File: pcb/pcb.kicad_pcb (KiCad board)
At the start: 2 copper layers, 145.2 x 98.5 mm, 105 parts, among them J1 OLED Connector, J2 Tag connect TC2030-CTX, J3 USB C 2.0 Connector, J4 Conn_01x01_Socket, J5 Conn_01x01_Socket, Q1 BSS84, Q2 BSS138, SW1 RESET, SW10 SW_Push, SW11 SW_Push, SW12 SW_Push, SW13 SW_Push, SW14 SW_Push, SW15 SW_Push, SW16 SW_Push, SW17 SW_Push, SW18 SW_Push, SW19 SW_Push, SW2 SW_Push, SW20 SW_Push, SW21 SW_Push, SW22 SW_Push, SW23 EC11 Encoder, SW24 ON/OFF, SW3 SW_Push, SW4 SW_Push, SW5 SW_Push, SW6 SW_Push, SW7 SW_Push, SW8 SW_Push, SW9 SW_Push, U1 nRF52840, U2 BQ24073RGT, U3 USBLC6-2SC6, U4 DRV2605LDGS, Y1 32MHz, Y2 32.768kHz

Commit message: finished routing second half
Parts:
- added AE2: Antenna_Shield, kbd:BLE_ANTENNA, B.Cu at (222.5, 141.9)
- added BT3: Lipo Cell, Connector_JST:JST_PH_S2B-PH-SM4-TB_1x02-1MP_P2.00mm_Horizontal, F.Cu at (241.9, 102.6)
- added C32: 1.2p, Capacitor_SMD:C_0402_1005Metric, F.Cu at (228.6, 141.5)
- added C33: 8p, Capacitor_SMD:C_0402_1005Metric, F.Cu at (232.3, 143.8)
- added C34: 8p, Capacitor_SMD:C_0402_1005Metric, F.Cu at (238.1, 142.1)
- added C35: 1p, Capacitor_SMD:C_0402_1005Metric, F.Cu at (230.7, 139.4)
- added C36: 8p, Capacitor_SMD:C_0402_1005Metric, F.Cu at (241.4, 132.8)
- added C37: 8p, Capacitor_SMD:C_0402_1005Metric, F.Cu at (240.1, 131.4)
- added C38: 100n, Capacitor_SMD:C_0402_1005Metric, F.Cu at (242.4, 134.6)
- added C40: 100p, Capacitor_SMD:C_0402_1005Metric, F.Cu at (231.9, 141.3)
- added C42: 47n, Capacitor_SMD:C_0402_1005Metric, F.Cu at (238.8, 137.0)
- added C43: 1u, Capacitor_SMD:C_0603_1608Metric, F.Cu at (240.1, 136.5)
- added C45: 4u7, Capacitor_SMD:C_0805_2012Metric, F.Cu at (233.1, 126.8)
- added C46: 1u, Capacitor_SMD:C_0603_1608Metric, F.Cu at (223.1, 118.0)
- added C47: 4u7, Capacitor_SMD:C_0805_2012Metric, F.Cu at (235.6, 128.4)
- added C48: 1u, Capacitor_SMD:C_0603_1608Metric, F.Cu at (236.6, 140.1)
- added C49: 100n, Capacitor_SMD:C_0402_1005Metric, F.Cu at (236.2, 130.0)
- added C50: 100n, Capacitor_SMD:C_0402_1005Metric, F.Cu at (229.2, 131.3)
- added C51: 100n, Capacitor_SMD:C_0402_1005Metric, F.Cu at (227.4, 133.8)
- added C52: 4u7, Capacitor_SMD:C_0805_2012Metric, F.Cu at (231.3, 128.0)
- added C53: 1u, Capacitor_SMD:C_0603_1608Metric, F.Cu at (232.6, 103.9)
- added C54: 4u7, Capacitor_SMD:C_0805_2012Metric, F.Cu at (228.3, 111.3)
- added C55: 4u7, Capacitor_SMD:C_0805_2012Metric, F.Cu at (235.4, 102.5)
- added C56: 100n, Capacitor_SMD:C_0402_1005Metric, F.Cu at (245.1, 108.6)
- added D43: 1N4148W, Diode_SMD:D_SOD-123, F.Cu at (252.9, 117.1)
- added D44: 1N4148W, Diode_SMD:D_SOD-123, F.Cu at (267.3, 115.5)
- added D45: 1N4148W, Diode_SMD:D_SOD-123, F.Cu at (286.1, 112.6)
- added D46: 1N4148W, Diode_SMD:D_SOD-123, F.Cu at (305.1, 112.7)
- added D47: 1N4148W, Diode_SMD:D_SOD-123, F.Cu at (324.1, 115.3)
- added D48: 1N4148W, Diode_SMD:D_SOD-123, F.Cu at (342.9, 115.9)
- added D49: 1N4148W, Diode_SMD:D_SOD-123, F.Cu at (253.3, 136.1)
- added D50: 1N4148W, Diode_SMD:D_SOD-123, F.Cu at (266.7, 134.7)
- added D51: 1N4148W, Diode_SMD:D_SOD-123, F.Cu at (285.5, 131.5)
- added D52: 1N4148W, Diode_SMD:D_SOD-123, F.Cu at (304.7, 132.1)
- added D53: 1N4148W, Diode_SMD:D_SOD-123, F.Cu at (323.9, 134.7)
- added D54: 1N4148W, Diode_SMD:D_SOD-123, F.Cu at (342.7, 134.7)
- added D55: 1N4148W, Diode_SMD:D_SOD-123, F.Cu at (248.4, 153.4)
- added D56: 1N4148W, Diode_SMD:D_SOD-123, F.Cu at (267.3, 153.5)
- added D57: 1N4148W, Diode_SMD:D_SOD-123, F.Cu at (286.1, 150.9)
- added D58: 1N4148W, Diode_SMD:D_SOD-123, F.Cu at (305.3, 151.3)
- added D59: 1N4148W, Diode_SMD:D_SOD-123, F.Cu at (324.1, 153.7)
- added D60: 1N4148W, Diode_SMD:D_SOD-123, F.Cu at (342.9, 153.9)
- added D61: 1N4148W, Diode_SMD:D_SOD-123, F.Cu at (227.9, 186.9)
- added D62: 1N4148W, Diode_SMD:D_SOD-123, F.Cu at (246.5, 178.9)
- added D63: 1N4148W, Diode_SMD:D_SOD-123, F.Cu at (266.9, 174.7)
- added H10: MountingHole, MountingHole:MountingHole_2.2mm_M2, F.Cu at (340.3, 141.7)
- added H6: MountingHole, MountingHole:MountingHole_2.2mm_M2, F.Cu at (238.8, 167.6)
- added H7: MountingHole, MountingHole:MountingHole_2.2mm_M2, F.Cu at (264.3, 105.7)
- added H8: MountingHole, MountingHole:MountingHole_2.2mm_M2, F.Cu at (264.3, 141.7)
- added H9: MountingHole, MountingHole:MountingHole_2.2mm_M2, F.Cu at (340.3, 105.7)
- added J10: Tag connect TC2030-CTX, Connector_PinHeader_2.54mm:PinHeader_2x03_P2.54mm_Vertical, F.Cu at (220.4, 130.0)
- added J11: USB C 2.0 Connector, kbd:TYPE-C-31-M-13C, F.Cu at (224.9, 99.1)
- added J7: OLED Connector, kbd:OLED, F.Cu at (231.8, 145.6)
- added J8: Conn_01x01_Socket, kbd:TE_2199248-6, F.Cu at (230.5, 118.9)
- added J9: Conn_01x01_Socket, kbd:TE_2199248-6, F.Cu at (231.4, 122.6)
- added L10: 2.2nH, Inductor_SMD:L_0402_1005Metric, F.Cu at (227.2, 142.1)
- added L4: 4.7nH, Inductor_SMD:L_0402_1005Metric, F.Cu at (229.3, 140.1)
- added L6: 10uH, Inductor_SMD:L_0603_1608Metric, F.Cu at (241.7, 135.8)
- added L7: 10uH, Inductor_SMD:L_0603_1608Metric, F.Cu at (234.5, 125.5)
- added L8: 15nH, Inductor_SMD:L_0402_1005Metric, F.Cu at (243.0, 137.4)
- added Q5: BSS84, Package_TO_SOT_SMD:SOT-23, F.Cu at (241.3, 109.1)
- added Q6: BSS138, Package_TO_SOT_SMD:SOT-23, F.Cu at (233.9, 113.9)
- added R21: 2k2, Resistor_SMD:R_0402_1005Metric, F.Cu at (223.3, 126.1)
- added R22: 2k2, Resistor_SMD:R_0402_1005Metric, F.Cu at (220.7, 119.6)
- added R23: 100k, Resistor_SMD:R_0603_1608Metric, F.Cu at (241.0, 111.7)
- added R24: 5k1, Resistor_SMD:R_0402_1005Metric, F.Cu at (226.9, 105.9)
- added R25: 5k1, Resistor_SMD:R_0402_1005Metric, F.Cu at (222.7, 105.9)
- added R26: 10k, Resistor_SMD:R_0402_1005Metric, F.Cu at (244.0, 108.6)
- added R27: 3k2, Resistor_SMD:R_0402_1005Metric, F.Cu at (234.5, 110.7)
- added R28: 10k, Resistor_SMD:R_0402_1005Metric, F.Cu at (246.3, 108.6)
- added R29: 5k9, Resistor_SMD:R_0402_1005Metric, F.Cu at (237.9, 109.3)
- added R30: 10k, Resistor_SMD:R_0402_1005Metric, F.Cu at (230.8, 109.2)
- added R31: 10k, Resistor_SMD:R_0402_1005Metric, F.Cu at (231.7, 110.0)
- added SW46: RESET, Button_Switch_SMD:SW_Push_SPST_NO_Alps_SKRK, F.Cu at (225.6, 127.4)
- added SW47: ON/OFF, Button_Switch_SMD:SW_SPDT_CK_JS102011SAQN, F.Cu at (218.7, 113.4)
- added SW48: EC11 Encoder, Rotary_Encoder:RotaryEncoder_Alps_EC11E-Switch_Vertical_H20mm_MountingHoles, F.Cu at (224.5, 152.6)
- added SW49: SW_Push, kbd:keyswitch_choc12_hotswap_1u, F.Cu at (254.5, 108.0)
- added SW50: SW_Push, kbd:keyswitch_choc12_hotswap_1u, F.Cu at (273.5, 108.0)
- added SW51: SW_Push, kbd:keyswitch_choc12_hotswap_1u, F.Cu at (292.6, 105.0)
- added SW52: SW_Push, kbd:keyswitch_choc12_hotswap_1u, F.Cu at (311.6, 105.5)
- added SW53: SW_Push, kbd:keyswitch_choc12_hotswap_1u, F.Cu at (330.7, 108.2)
- added SW54: SW_Push, kbd:keyswitch_choc12_hotswap_1u, F.Cu at (349.7, 108.2)
- added SW55: SW_Push, kbd:keyswitch_choc12_hotswap_1u, F.Cu at (254.5, 127.1)
- added SW56: SW_Push, kbd:keyswitch_choc12_hotswap_1u, F.Cu at (273.5, 127.1)
- added SW57: SW_Push, kbd:keyswitch_choc12_hotswap_1u, F.Cu at (292.6, 124.0)
- added SW58: SW_Push, kbd:keyswitch_choc12_hotswap_1u, F.Cu at (311.6, 124.5)
- added SW59: SW_Push, kbd:keyswitch_choc12_hotswap_1u, F.Cu at (330.7, 127.3)
- added SW60: SW_Push, kbd:keyswitch_choc12_hotswap_1u, F.Cu at (349.7, 127.3)
- added SW61: SW_Push, kbd:keyswitch_choc12_hotswap_1u, F.Cu at (254.5, 146.1)
- added SW62: SW_Push, kbd:keyswitch_choc12_hotswap_1u, F.Cu at (273.5, 146.1)
- added SW63: SW_Push, kbd:keyswitch_choc12_hotswap_1u, F.Cu at (292.6, 143.1)
- added SW64: SW_Push, kbd:keyswitch_choc12_hotswap_1u, F.Cu at (311.6, 143.6)
- added SW65: SW_Push, kbd:keyswitch_choc12_hotswap_1u, F.Cu at (330.7, 146.3)
- added SW66: SW_Push, kbd:keyswitch_choc12_hotswap_1u, F.Cu at (349.7, 146.3)
- added SW67: SW_Push, kbd:keyswitch_choc12_hotswap_1u, F.Cu at (230.7, 177.3)
- added SW68: SW_Push, kbd:keyswitch_choc12_hotswap_1u, F.Cu at (251.2, 169.6)
- added SW69: SW_Push, kbd:keyswitch_choc12_hotswap_1u, F.Cu at (273.5, 167.0)
- added TH3: 10k, Resistor_SMD:R_0402_1005Metric, F.Cu at (264.5, 116.6)
- added TP2: TestPoint, TestPoint:TestPoint_Pad_2.0x2.0mm, F.Cu at (218.3, 121.2)
- added U10: USBLC6-2SC6, Package_TO_SOT_SMD:SOT-23-6, F.Cu at (225.0, 108.9)
- added U4: DRV2605LDGS, Package_SO:VSSOP-10_3x3mm_P0.5mm, F.Cu at (224.7, 120.8)
- added U7: nRF52840, Package_DFN_QFN:Nordic_AQFN-73-1EP_7x7mm_P0.5mm, F.Cu at (233.3, 134.9)
- added U9: BQ24073RGT, Package_DFN_QFN:VQFN-16-1EP_3x3mm_P0.5mm_EP1.6x1.6mm, F.Cu at (235.5, 107.7)
- added Y3: 32MHz, Crystal:Crystal_SMD_3225-4Pin_3.2x2.5mm, F.Cu at (234.6, 142.4)
- added Y4: 32.768kHz, Crystal:Crystal_SMD_3215-2Pin_3.2x1.5mm, F.Cu at (239.4, 133.1)
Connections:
- U1 pad B19: ~{CHG} -> ROW 0
- U1 pad J24: ROW 0 -> ~{CHG}
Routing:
- net ROW 1: track 172.3 -> 357.3 mm, vias 6 -> 15
- net ROW 2: track 191.3 -> 367.6 mm, vias 14 -> 27
- net COL 0: track 0.00 -> 165.7 mm, vias 0 -> 2
- net ROW 3: track 216.1 -> 372.1 mm, vias 16 -> 30
- net COL 1: track 0.00 -> 145.2 mm, vias 0 -> 2
- net COL 3: track 0.00 -> 141.9 mm, vias 0 -> 2
- net COL 2: track 0.00 -> 128.5 mm, vias 0 -> 2
- net COL 4: track 0.00 -> 123.2 mm, vias 0 -> 2
- net COL 5: track 0.00 -> 108.1 mm, vias 0 -> 2
- net ROW 0: track 100.1 -> 205.8 mm, vias 2 -> 4
- net VDD: track 94.7 -> 177.1 mm, vias 9 -> 16
- net Net-(U9-TS): track 0.00 -> 48.8 mm, vias 0 -> 2
- net VBAT_SENSE: track 39.2 -> 87.1 mm
- net ~{PGOOD}: track 24.7 -> 70.9 mm, vias 2 -> 6
- net ~{CHG}: track 30.6 -> 74.1 mm, vias 2 -> 6
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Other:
- board size 145.2 x 98.5 mm -> 296 x 98.6 mm

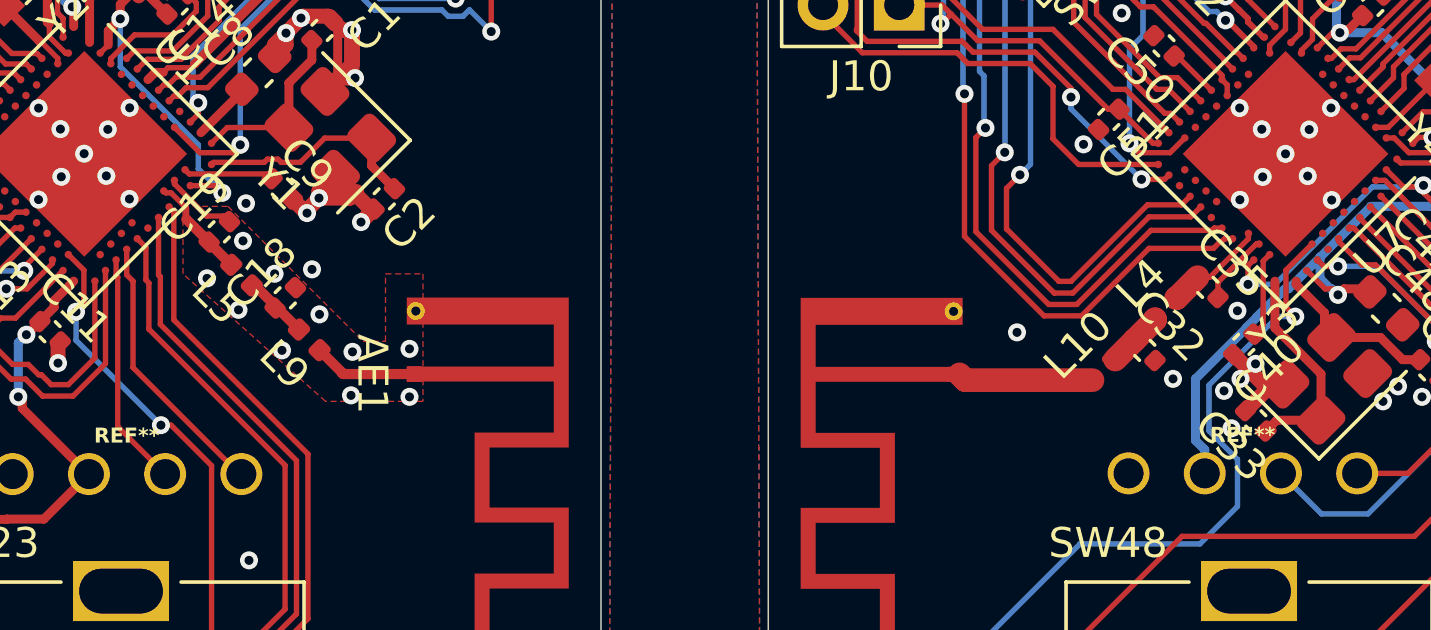
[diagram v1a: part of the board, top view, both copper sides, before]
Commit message: impedence matched 50ohms and adjusted pi network
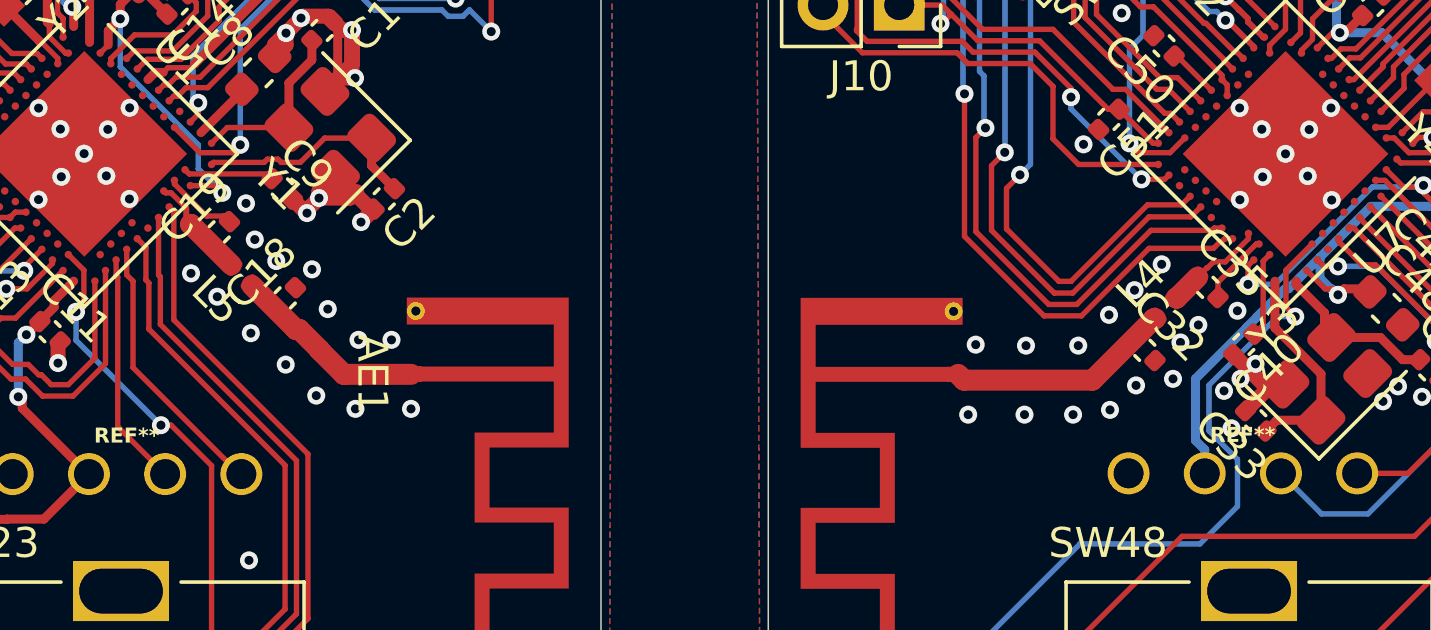
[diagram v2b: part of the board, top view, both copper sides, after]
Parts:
- removed L10, L9: 2.2nH, Inductor_SMD:L_0402_1005Metric
- C18, C32: value 1.2p -> 0.5pF
- C19, C35: value 1p -> 0.8pF
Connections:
- C18 pad 1: Net-(C18-Pad1) -> Net-(AE1-A)
- C32 pad 1: Net-(C32-Pad1) -> Net-(AE2-A)
- L4 pad 1: Net-(C32-Pad1) -> Net-(AE2-A)
- L5 pad 1: Net-(C18-Pad1) -> Net-(AE1-A)
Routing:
- net Net-(AE1-A): track 3.49 -> 6.55 mm
- net Net-(AE2-A): track 4.51 -> 7.51 mm
- net Net-(C18-Pad1): track 2.18 -> 0.00 mm
- net Net-(C32-Pad1): track 1.90 -> 0.00 mm
- net GND: vias 150 -> 164
